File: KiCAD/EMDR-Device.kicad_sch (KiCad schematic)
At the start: 32 parts, among them J1 USB_C_Receptacle_USB2.0_16P, U2 RP2350A, U5 W25Q128JVS, U6 XC6206PxxxMR, Y1 Crystal_GND24_Small

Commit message: schematic
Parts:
- removed C10, C20, C21, C22: 4.7uF, symbol Device:C_Small
- removed C11, C12, C13, C14, C15, C16, C17, C18, C19, C23, C8, C9: 100nF, symbol Device:C_Small
- removed C24, C25: 15pF, symbol Device:C_Small
- removed J1: USB_C_Receptacle_USB2.0_16P, symbol Connector:USB_C_Receptacle_USB2.0_16P
- removed L2: 3.3uF, symbol Device:L_45deg
- removed R10: 1k, symbol Device:R_Small
- removed R7, R8: 27, symbol Device:R_Small
- removed R9: 33, symbol Device:R_Small
- removed U2: RP2350A, Package_DFN_QFN:QFN-60-1EP_7x7mm_P0.4mm_EP3.4x3.4mm, symbol MCU_RaspberryPi:RP2350A
- removed U5: W25Q128JVS, Package_SO:SOIC-8_5.3x5.3mm_P1.27mm, symbol Memory_Flash:W25Q128JVS
- removed Y1: Crystal_GND24_Small, snapeda:XTAL_ABM8-272-T3, symbol Device:Crystal_GND24_Small
- added J1: USB_C_Receptacle_USB2.0_14P, Connector_USB:USB_C_Receptacle_HCTL_HC-TYPE-C-16P-01A, symbol Connector:USB_C_Receptacle_USB2.0_14P
- added R12, R13: 10k, Resistor_SMD:R_0603_1608Metric, symbol Device:R_Small
- added U2: ESP32-C6-MINI-1, RF_Module:ESP32-C6-MINI-1, symbol RF_Module:ESP32-C6-MINI-1
- C4, C7: footprint (none) -> Capacitor_SMD:C_0603_1608Metric
- R5, R6: footprint (none) -> Resistor_SMD:R_0603_1608Metric
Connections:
- net +3V3: now also R12.1, R13.2, U2.3 (3V3)
- net +5V: now also J1.A4 (VBUS), J1.A9 (VBUS), J1.B4 (VBUS), J1.B9 (VBUS); no longer C4.1, U6.3 (VI)
- net D_N: now also J1.A7 (D-), J1.B7 (D-), U2.17 (IO12)
- net D_P: now also J1.A6 (D+), J1.B6 (D+), U2.18 (IO13)
- net GND: now also J1.A1 (GND), J1.A12 (GND), J1.B1 (GND), J1.B12 (GND), J1.SH (SHIELD), U2.1 (GND), U2.11 (GND), U2.14 (GND), U2.2 (GND), U2.36 (GND), U2.37 (GND), U2.38 (GND), U2.39 (GND), U2.40 (GND), U2.41 (GND), U2.42 (GND), U2.43 (GND), U2.44 (GND), U2.45 (GND), U2.46 (GND), U2.47 (GND), U2.48 (GND), U2.49 (GND), U2.50 (GND), U2.51 (GND), U2.52 (GND), U2.53 (GND)
- net at R6.2: now also J1.B5 (CC2)
- net at R5.1: now also J1.A5 (CC1)
- new net BAT: U2.9 (IO4)
- new net EN: U2.8 (EN)
- new net V_SYS: C4.1, U6.3 (VI)
- new net i2c_scl: R13.1, U2.12 (IO0)
- new net i2c_sda: R12.2, U2.13 (IO1)
- no-connect marks 2 -> 0
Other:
- sheet BMS renamed Power
- removed sheet Wireless
- added sheet I2C multiplexer (subsheets/i2c_multiplexer.kicad_sch)
- added sheet IMU (subsheets/imu.kicad_sch)
- added sheet Mounting Holes (subsheets\mounting_holes.kicad_sch)
- sheet Power: file subsheets/bms.kicad_sch -> subsheets/power.kicad_sch
- note added: "ESP32 C6 MINI"
- note removed: "Crystal"
- note removed: "Decoupling Capacitors"
- note removed: "Flash"
- note removed: "RP2350A"
- moved on the sheet: C4, C7, R5, R6, U6

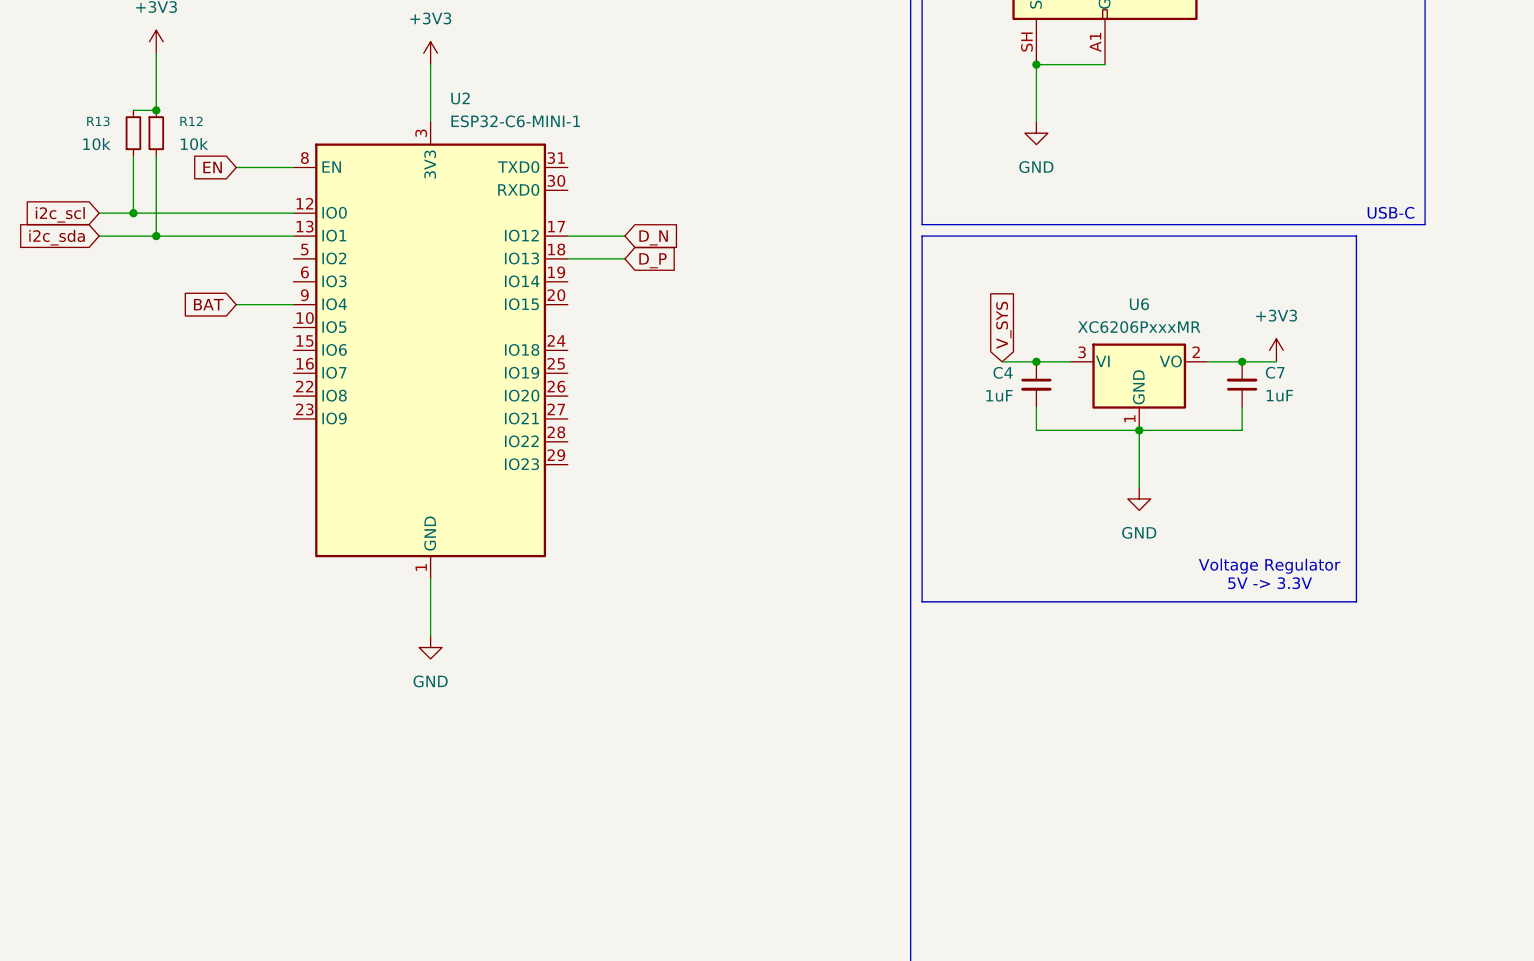
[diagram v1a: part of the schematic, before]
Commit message: connect forgotten pins
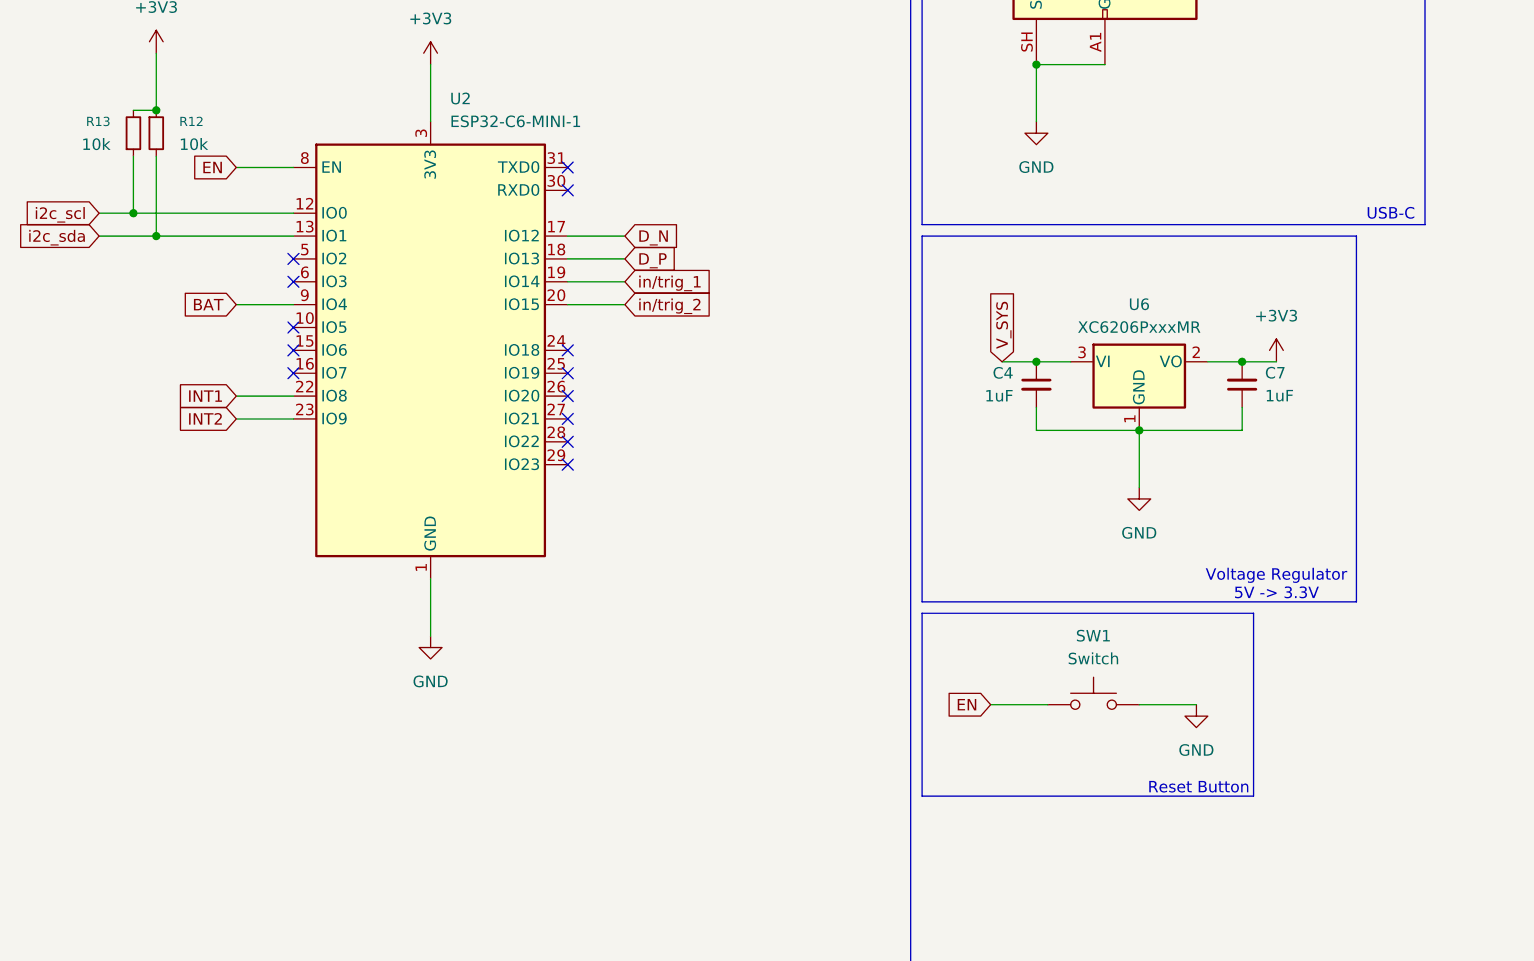
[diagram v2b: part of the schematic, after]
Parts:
- added SW1: Switch, chinh4thepro:reset_switch_smd_side, symbol ScottoKeebs:Placeholder_Switch
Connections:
- net EN: now also SW1.1
- net GND: now also SW1.2
- net in/trig_1: now reaches U2.19 (IO14)
- net in/trig_2: now reaches U2.20 (IO15)
- net INT1: now reaches U2.22 (IO8)
- net INT2: now reaches U2.23 (IO9)
- no-connect marks 0 -> 13
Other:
- sheet Mounting Holes: file subsheets\mounting_holes.kicad_sch -> subsheets/mounting_holes.kicad_sch
- note added: "Reset Button"

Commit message: preliminary pcb
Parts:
- added C12: 1uF, Capacitor_SMD:C_0603_1608Metric, symbol Device:C_Small
- added C17: 15pF, Capacitor_SMD:C_0603_1608Metric, symbol Device:C_Small
- added R14: 5.1k, Resistor_SMD:R_0603_1608Metric, symbol Device:R_Small
- added R15, R16: 10k, Resistor_SMD:R_0603_1608Metric, symbol Device:R_Small
- added SW2: Switch, Button_Switch_SMD:Panasonic_EVQPUJ_EVQPUA, symbol ScottoKeebs:Placeholder_Switch
- SW1: footprint chinh4thepro:reset_switch_smd_side -> Button_Switch_SMD:Panasonic_EVQPUJ_EVQPUA
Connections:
- net +3V3: now also R14.1, R15.2, R16.2
- net EN: now also C12.2, R15.1
- net GND: now also C12.1, C17.1, SW2.2
- net INT1: now also U2.5 (IO2); no longer U2.22 (IO8)
- net INT2: now also U2.6 (IO3); no longer U2.23 (IO9)
- new net: R14.2, U2.22 (IO8)
- new net BOOT: C17.2, R16.1, SW2.1, U2.23 (IO9)
- no-connect marks 13 -> 11
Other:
- note added: "Boot Button"
- moved on the sheet: SW1
